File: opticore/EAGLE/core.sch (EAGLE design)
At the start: 67 parts, among them IC2 MC33269T-5.0, J1 POWER_JACKSLT, Q1 2N3904, Q2 2N3904, Q3 2N3904, Q4 2N3904, Q5 2N3904, Q6 2N3904, Q7 2N3904, X1 FFKV8

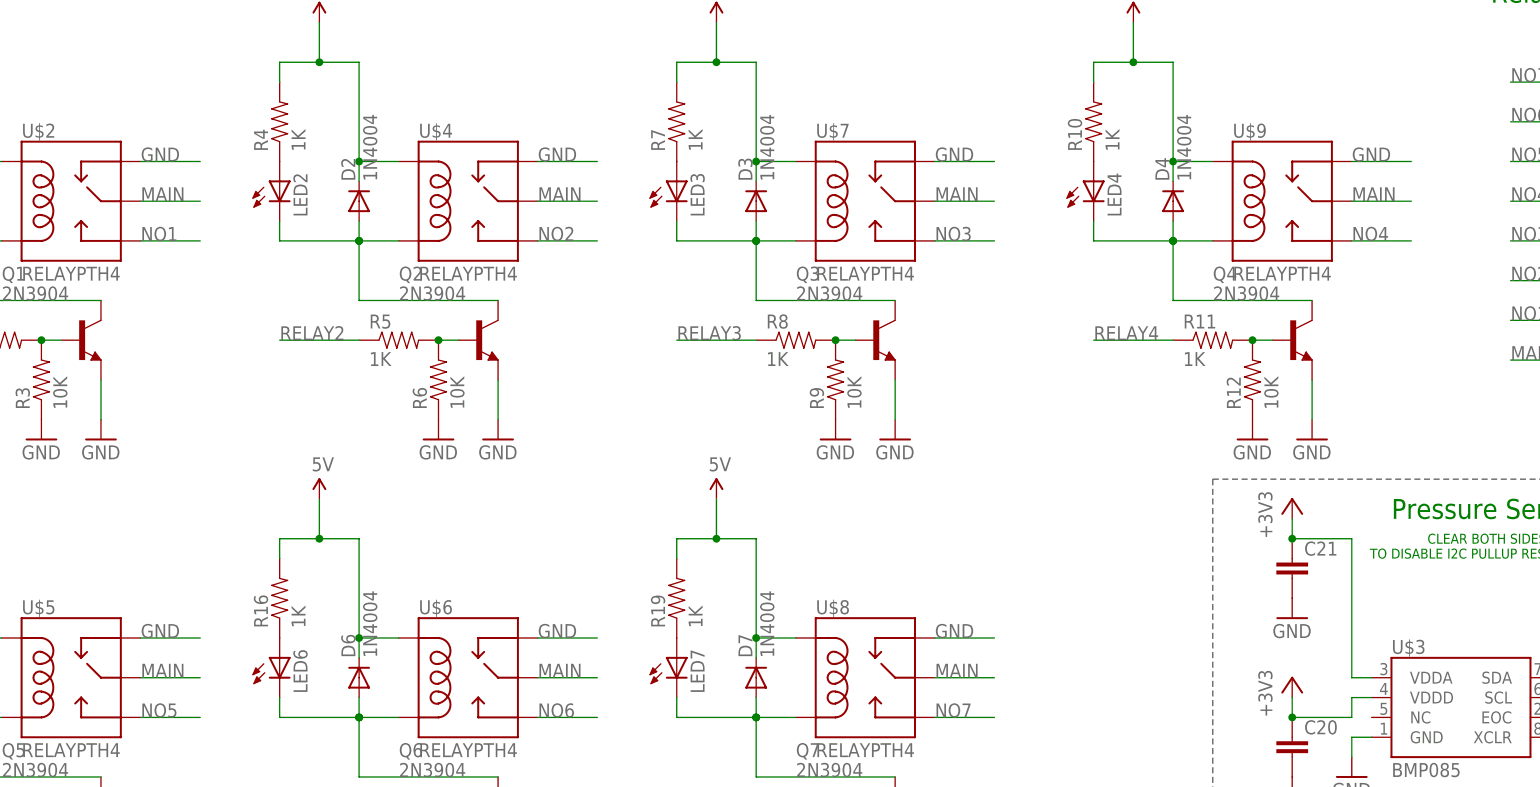
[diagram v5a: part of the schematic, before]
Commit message: Major fix with relays
The previous version would break everything.

Signed-off-by: Scott Lerner <scottphiliplerner@gmail.com>
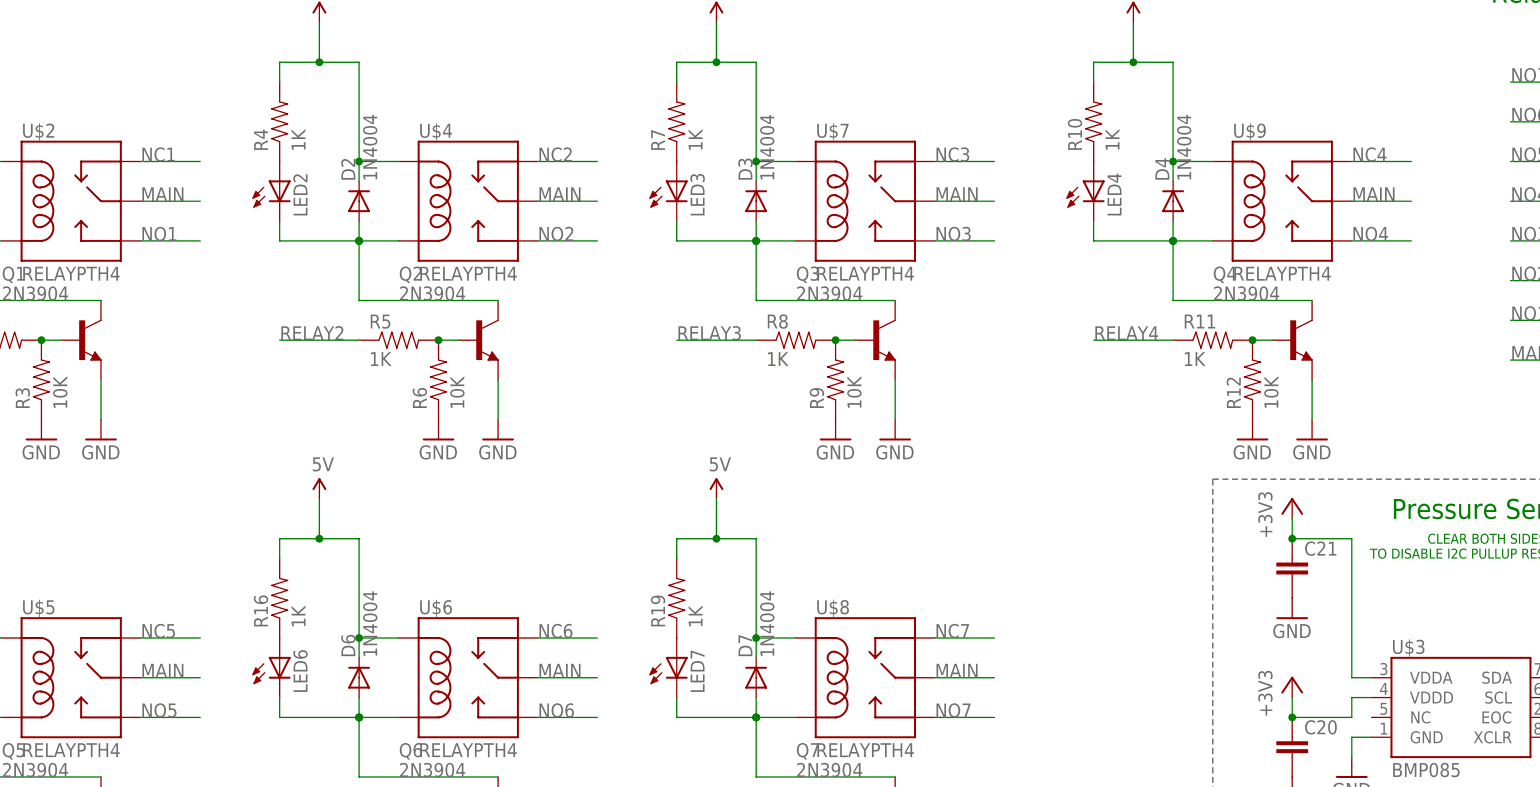
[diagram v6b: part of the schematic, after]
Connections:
- new net NC1: U$2.NC
- new net NC2: U$4.NC
- new net NC3: U$7.NC
- new net NC4: U$9.NC
- new net NC5: U$5.NC
- new net NC6: U$6.NC
- new net NC7: U$8.NC
- net GND: no longer U$2.NC, U$4.NC, U$5.NC, U$6.NC, U$7.NC, U$8.NC, U$9.NC
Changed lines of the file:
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@@
 <pinref part="R21" gate="G$1" pin="1"/>
-</segment>
-<segment>
-<pinref part="U$2" gate="G$1" pin="NC"/>
-<wire x1="43.18" y1="157.48" x2="50.8" y2="157.48" width="0.1524" layer="91"/>
-<label x="43.18" y="157.48" size="1.778" layer="95"/>
-</segment>
-<segment>
-<pinref part="U$4" gate="G$1" pin="NC"/>
-<wire x1="93.98" y1="157.48" x2="101.6" y2="157.48" width="0.1524" layer="91"/>
-<label x="93.98" y="157.48" size="1.778" layer="95"/>
-</segment>
-<segment>
-<pinref part="U$7" gate="G$1" pin="NC"/>
-<wire x1="144.78" y1="157.48" x2="152.4" y2="157.48" width="0.1524" layer="91"/>
-<label x="144.78" y="157.48" size="1.778" layer="95"/>
-</segment>
-<segment>
-<pinref part="U$9" gate="G$1" pin="NC"/>
-<wire x1="198.12" y1="157.48" x2="205.74" y2="157.48" width="0.1524" layer="91"/>
-<label x="198.12" y="157.48" size="1.778" layer="95"/>
-</segment>
-<segment>
-<pinref part="U$8" gate="G$1" pin="NC"/>
-<wire x1="144.78" y1="96.52" x2="152.4" y2="96.52" width="0.1524" layer="91"/>
-<label x="144.78" y="96.52" size="1.778" layer="95"/>
-</segment>
-<segment>
-<pinref part="U$6" gate="G$1" pin="NC"/>
-<wire x1="93.98" y1="96.52" x2="101.6" y2="96.52" width="0.1524" layer="91"/>
-<label x="93.98" y="96.52" size="1.778" layer="95"/>
-</segment>
-<segment>
-<pinref part="U$5" gate="G$1" pin="NC"/>
-<wire x1="43.18" y1="96.52" x2="50.8" y2="96.52" width="0.1524" layer="91"/>
-<label x="43.18" y="96.52" size="1.778" layer="95"/>
 </segment>
 </net>
@@
 </segment>
 </net>
+<net name="NC1" class="1">
+<segment>
+<pinref part="U$2" gate="G$1" pin="NC"/>
+<wire x1="43.18" y1="157.48" x2="50.8" y2="157.48" width="0.1524" layer="91"/>
+<label x="43.18" y="157.48" size="1.778" layer="95"/>
+</segment>
+</net>
+<net name="NC2" class="1">
+<segment>
+<pinref part="U$4" gate="G$1" pin="NC"/>
+<wire x1="93.98" y1="157.48" x2="101.6" y2="157.48" width="0.1524" layer="91"/>
+<label x="93.98" y="157.48" size="1.778" layer="95"/>
+</segment>
+</net>
+<net name="NC3" class="1">
+<segment>
+<pinref part="U$7" gate="G$1" pin="NC"/>
+<wire x1="144.78" y1="157.48" x2="152.4" y2="157.48" width="0.1524" layer="91"/>
+<label x="144.78" y="157.48" size="1.778" layer="95"/>
+</segment>
+</net>
+<net name="NC4" class="1">
+<segment>
+<pinref part="U$9" gate="G$1" pin="NC"/>
+<wire x1="198.12" y1="157.48" x2="205.74" y2="157.48" width="0.1524" layer="91"/>
+<label x="198.12" y="157.48" size="1.778" layer="95"/>
+</segment>
+</net>
+<net name="NC5" class="1">
+<segment>
+<pinref part="U$5" gate="G$1" pin="NC"/>
+<wire x1="43.18" y1="96.52" x2="50.8" y2="96.52" width="0.1524" layer="91"/>
+<label x="43.18" y="96.52" size="1.778" layer="95"/>
+</segment>
+</net>
+<net name="NC6" class="1">
+<segment>
+<pinref part="U$6" gate="G$1" pin="NC"/>
+<wire x1="93.98" y1="96.52" x2="101.6" y2="96.52" width="0.1524" layer="91"/>
+<label x="93.98" y="96.52" size="1.778" layer="95"/>
+</segment>
+</net>
+<net name="NC7" class="1">
+<segment>
+<pinref part="U$8" gate="G$1" pin="NC"/>
+<wire x1="144.78" y1="96.52" x2="152.4" y2="96.52" width="0.1524" layer="91"/>
+<label x="144.78" y="96.52" size="1.778" layer="95"/>
+</segment>
+</net>

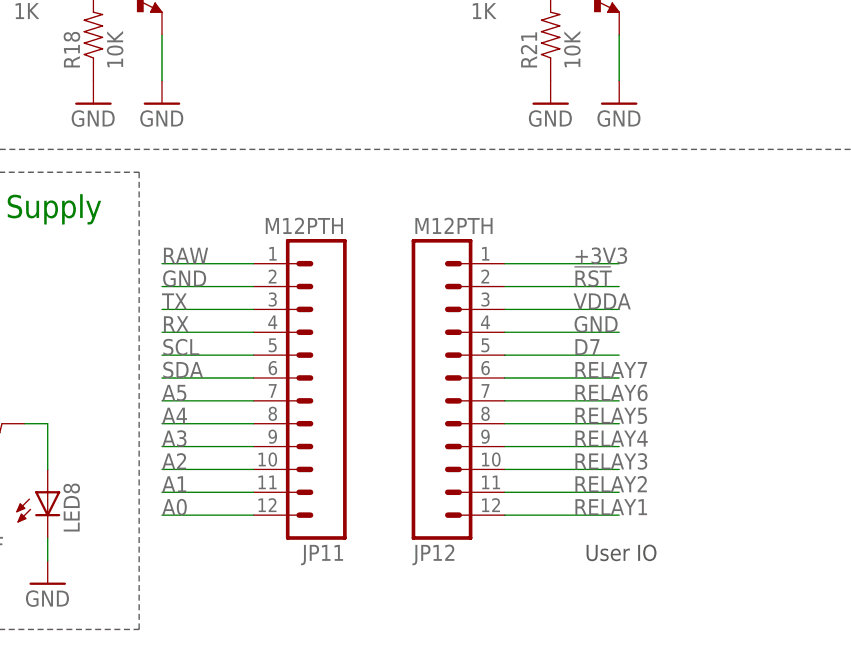
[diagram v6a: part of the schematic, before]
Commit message: Rewiring some things
Still haven't implemented 24V power supply.
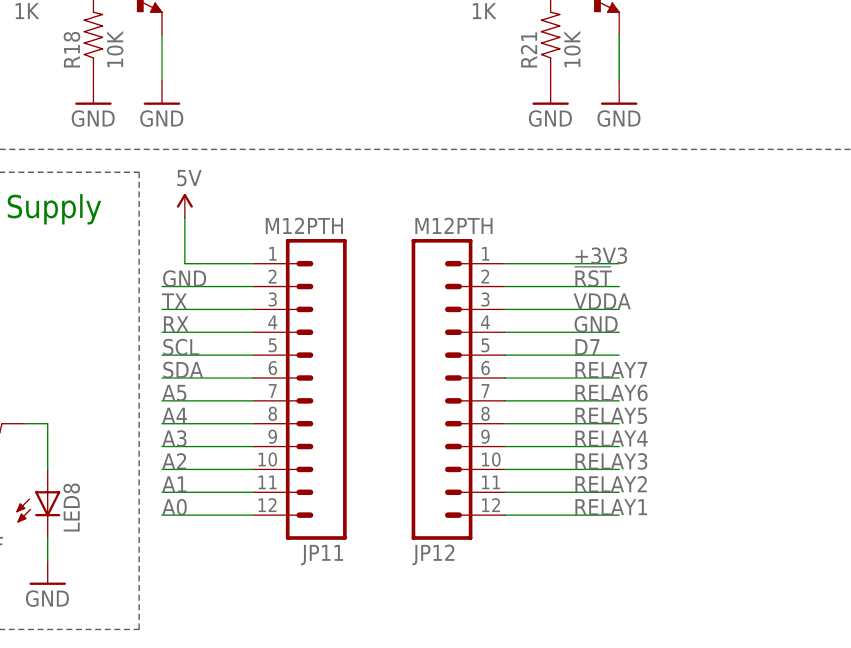
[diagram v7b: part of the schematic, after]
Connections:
- removed net RAW: JP11.1
- net 5V: now also JP11.1
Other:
- note removed: "User IO"
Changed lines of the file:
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@@
 <part name="LED7" library="SparkFun-LED" deviceset="LED" device="3MM"/>
 <part name="LED8" library="SparkFun-LED" deviceset="LED" device="3MM"/>
+<part name="SUPPLY9" library="SparkFun-Aesthetics" deviceset="5V" device=""/>
 </parts>
 <sheets>
@@
 <text x="228.6" y="106.68" size="1.27" layer="91" align="bottom-right">CLEAR BOTH SIDES OF SJ1
 TO DISABLE I2C PULLUP RESISTORS</text>
-<text x="135.89" y="10.16" size="1.778" layer="97">User IO</text>
 </plain>
 <instances>
@@
 <instance part="LED7" gate="G$1" x="111.76" y="93.98"/>
 <instance part="LED8" gate="G$1" x="76.2" y="17.78"/>
+<instance part="SUPPLY9" gate="G$1" x="91.44" y="48.26"/>
 </instances>
 <busses>
@@
 <pinref part="GND36" gate="1" pin="GND"/>
 <pinref part="R21" gate="G$1" pin="1"/>
-</segment>
-</net>
-<net name="RAW" class="1">
-<segment>
-<wire x1="99.06" y1="43.18" x2="88.9" y2="43.18" width="0.1524" layer="91"/>
-<label x="88.9" y="43.18" size="1.778" layer="95"/>
-<pinref part="JP11" gate="G$1" pin="1"/>
 </segment>
 </net>
@@
 <junction x="63.5" y="25.4"/>
 </segment>
-</net>
+<segment>
+<pinref part="JP11" gate="G$1" pin="1"/>
+<pinref part="SUPPLY9" gate="G$1" pin="5V"/>
+<wire x1="99.06" y1="43.18" x2="91.44" y2="43.18" width="0.1524" layer="91"/>
+<wire x1="91.44" y1="43.18" x2="91.44" y2="48.26" width="0.1524" layer="91"/>
+</segment>
+</net>

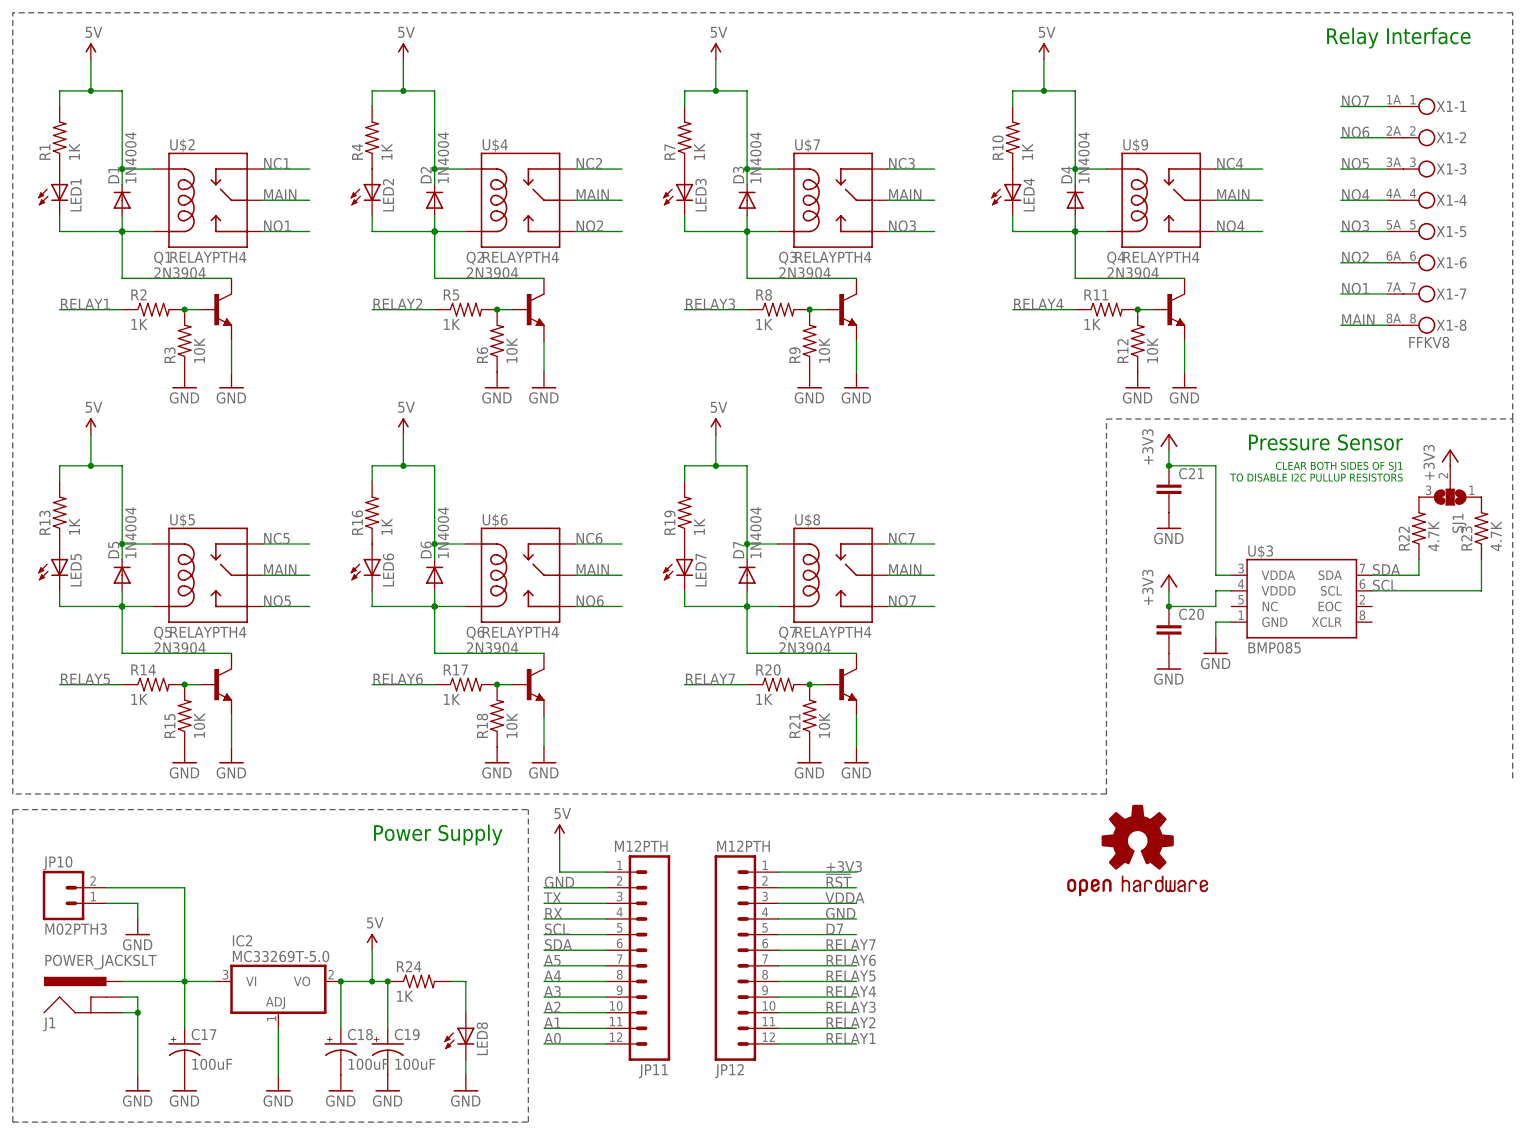
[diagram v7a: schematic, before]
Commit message: Upgrading to power supply that will work
Proven method from previous designs.
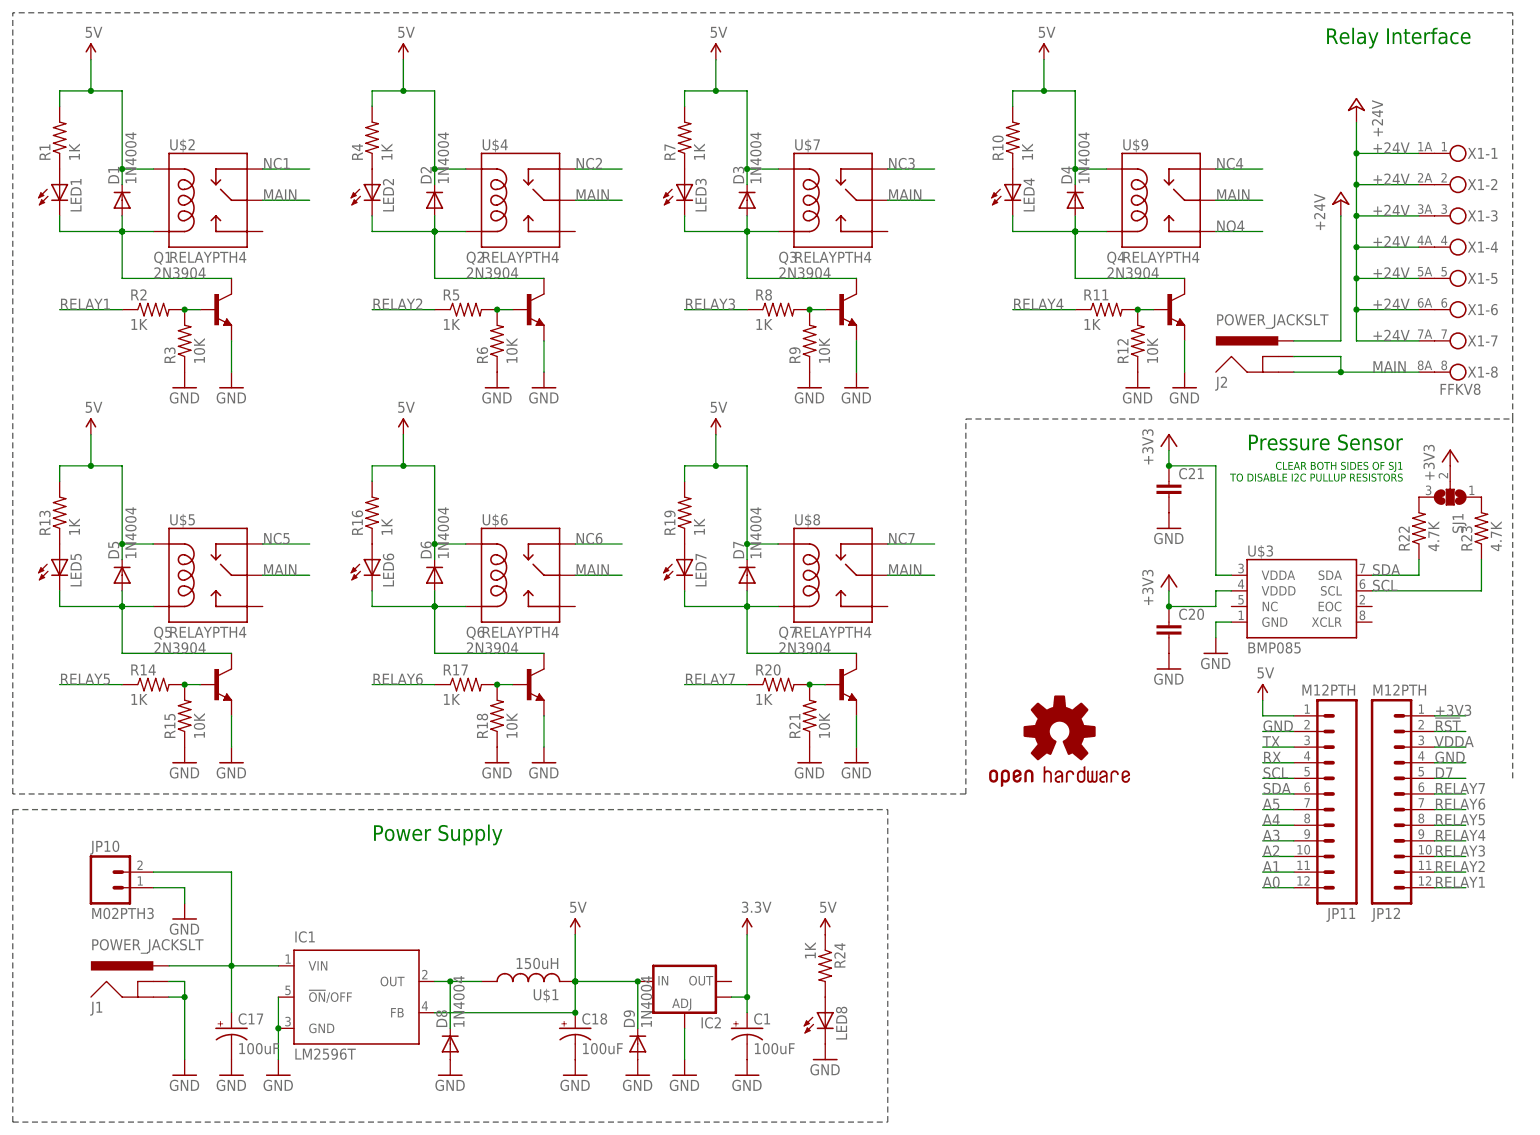
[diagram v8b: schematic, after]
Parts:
- removed C19: 100uF, SparkFun-Passives:CAP_POLPTH1
- added C1: 100uF, SparkFun-Passives:CAP_POLPTH1
- added D8, D9: 1N4004, diode:1N4004
- added IC1: LM2596T, national-semiconductor:LM2596T
- added J2: POWER_JACKSLT, SparkFun-Connectors:POWER_JACKSLT
- added U$1: 150uH, adafruit:L
- IC2: value MC33269T-5.0 -> (none); device linear:MC33269T-5.0 -> SparkFun-PowerIC:V_REG_LM1117SOT223
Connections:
- removed net NO1: U$2.NO, X1-7.2
- removed net NO2: U$4.NO, X1-6.2
- removed net NO3: U$7.NO, X1-5.2
- removed net NO5: U$5.NO, X1-3.2
- removed net NO6: U$6.NO, X1-2.2
- removed net NO7: U$8.NO, X1-1.2
- new net +24V: J2.PWR, X1-1.2, X1-2.2, X1-3.2, X1-4.2, X1-5.2, X1-6.2, X1-7.2
- new net 3.3V: C1.+, IC2.OUT@1
- new net N$10: D8.C, IC1.OUT, U$1.1
- net 5V: now also D9.C, IC1.FB, IC2.IN, U$1.2; no longer C19.+, IC2.VO
- net GND: now also C1.-, D8.A, D9.A, IC1.!ON!/OFF, IC1.GND; no longer C19.-
- net MAIN: now also J2.GND, J2.GNDBREAK
- net N$37: now also IC1.VIN; no longer IC2.VI
- net NO4: no longer X1-4.2
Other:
- moved on the sheet: C17, C18, J1, JP10, JP11, JP12, LED8, R24, X1-1, X1-2, X1-3, X1-4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
